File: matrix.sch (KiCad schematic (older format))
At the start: 134 parts, among them SW1 SW_Push, SW10 SW_Push, SW11 SW_Push, SW12 SW_Push, SW13 SW_Push, SW14 SW_Push, SW15 SW_Push, SW16 SW_Push, SW17 SW_Push, SW18 SW_Push, SW19 SW_Push, SW2 SW_Push, SW20 SW_Push, SW21 SW_Push, SW22 SW_Push, SW23 SW_Push, SW24 SW_Push, SW25 SW_Push, SW26 SW_Push, SW27 SW_Push, SW28 SW_Push, SW29 SW_Push, SW3 SW_Push, SW30 SW_Push, SW31 SW_Push, SW32 SW_Push, SW33 SW_Push, SW34 SW_Push, SW35 SW_Push, SW36 SW_Push, SW37 SW_Push, SW38 SW_Push, SW39 SW_Push, SW4 SW_Push, SW40 SW_Push, SW41 SW_Push, SW42 SW_Push, SW43 SW_Push, SW44 SW_Push, SW45 SW_Push, SW46 SW_Push, SW47 SW_Push, SW48 SW_Push, SW49 SW_Push, SW5 SW_Push, SW50 SW_Push, SW51 SW_Push, SW52 SW_Push, SW53 SW_Push, SW54 SW_Push, SW55 SW_Push, SW56 SW_Push, SW57 SW_Push, SW58 SW_Push, SW59 SW_Push, SW6 SW_Push, SW60 SW_Push, SW61 SW_Push, SW62 SW_Push, SW63 SW_Push, SW64 SW_Push, SW65 SW_Push, SW66 SW_Push, SW67 SW_Push, SW7 SW_Push, SW8 SW_Push, SW9 SW_Push

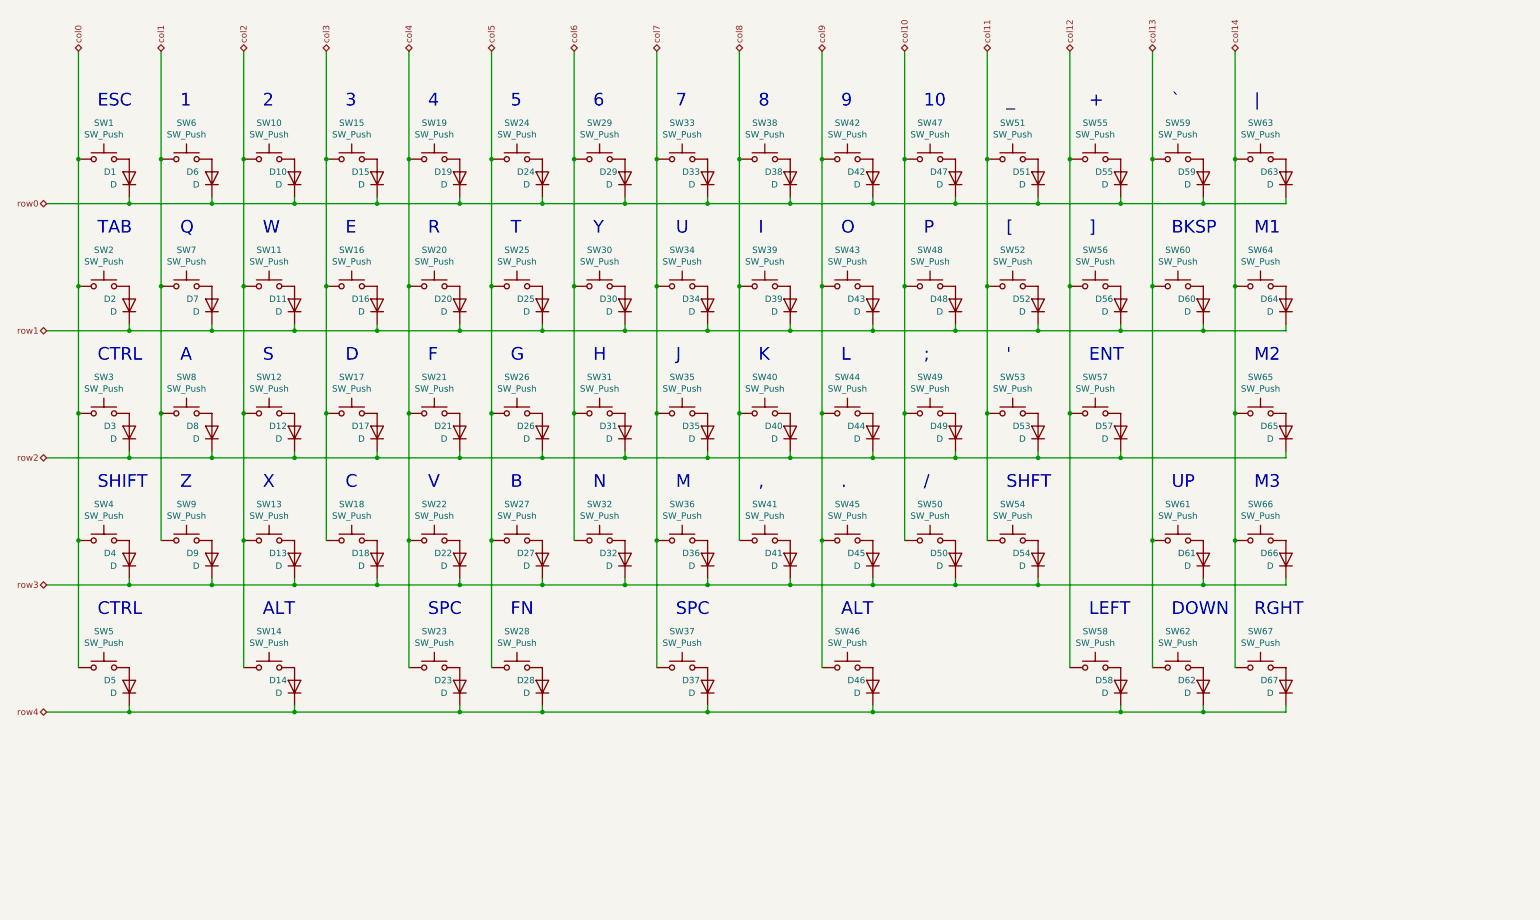
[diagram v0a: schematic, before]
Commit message: Initial project update
- Imported FateParts library
- Updated schematic with full backspace switch and stepped capslock switch
- Added new switch footprints to layout
- Updated some traces in layout
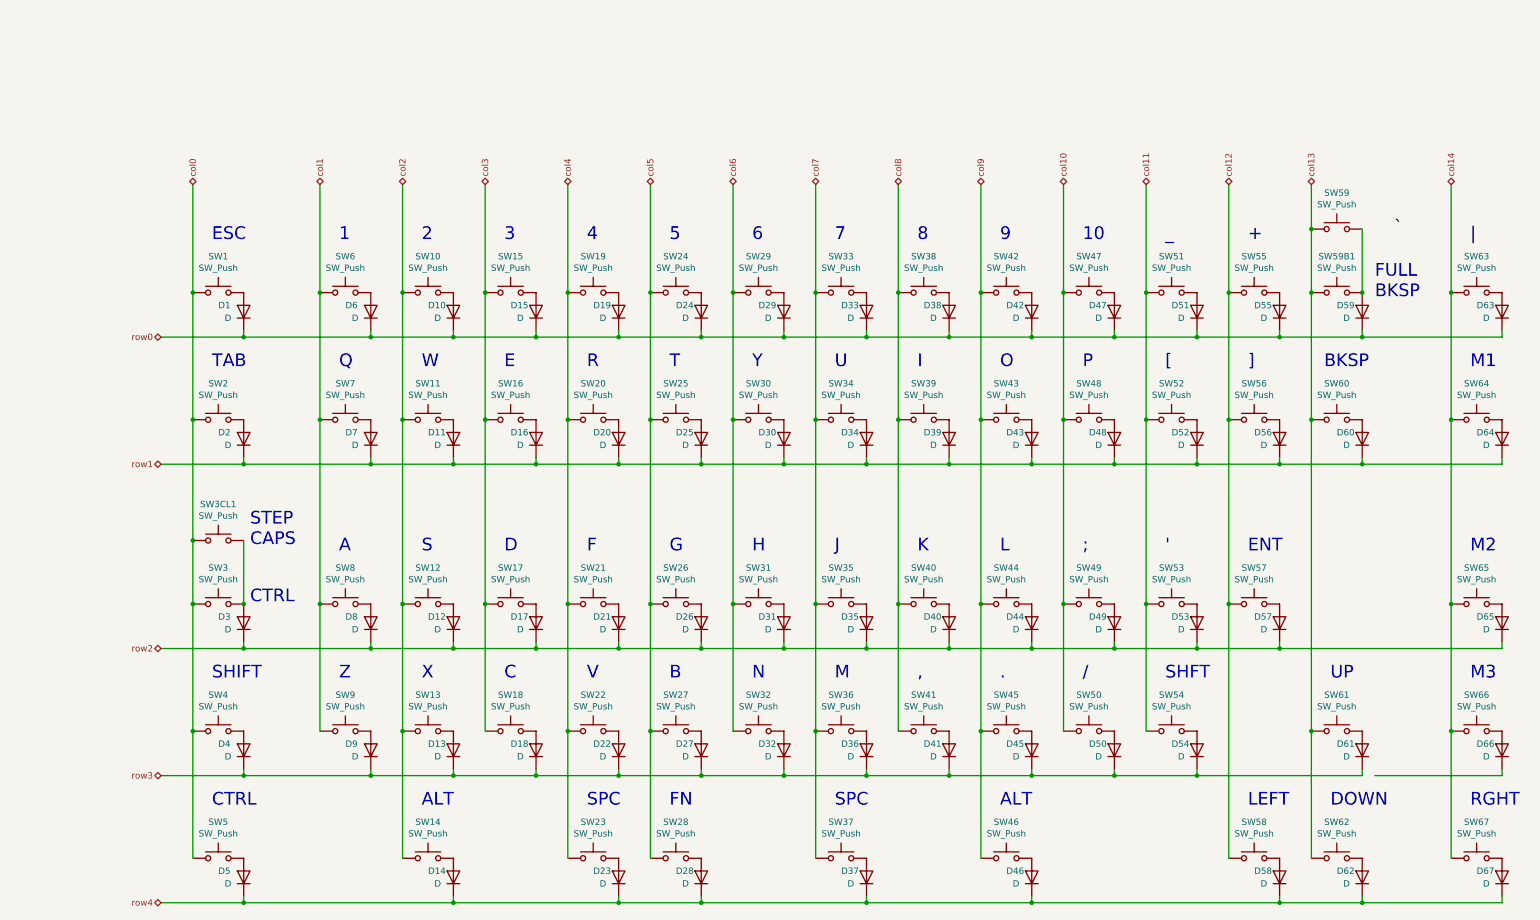
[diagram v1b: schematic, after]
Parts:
- added SW3CL1: SW_Push, FateParts-MXSwitch:SW_Cherry_MX_1.25u_PCB, symbol Switch:SW_Push
- added SW59B1: SW_Push, FateParts-MXSwitch:SW_Cherry_MX_2.00u_PCB, symbol Switch:SW_Push
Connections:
- net col0: now also SW3CL1.1
- net col13: now also SW59B1.1
- net row3: no longer D66.1 (K)
- net at D3.2 (A), SW3.2: now also SW3CL1.2
- net at D59.2 (A), SW59.2: now also SW59B1.2
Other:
- note added: "FULL\nBKSP"
- note added: "STEP\nCAPS"
- moved on the sheet: D1, D10, D11, D12, D13, D14, D15, D16, D17, D18, D19, D2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

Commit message: Addition of BOM and position files
- Added JLCPCB part numbers in BOM and exported
- Exported component positioning file
- Some minor cleanup of traces and silkscreen legend positions.
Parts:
- D1, D10, D11, D12, D13, D14, D15, D16, D17, D18, D19, D2, D20, D21, D22, D23, D24, D25, D26, D27, D28, D29, D3, D30, D31, D32, D33, D34, D35, D36, D37, D38, D39, D4, D40, D41, D42, D43, D44, D45, D46, D47, D48, D49, D5, D50, D51, D52, D53, D54, D55, D56, D57, D58, D59, D6, D60, D61, D62, D63, D64, D65, D66, D67, D7, D8, D9: LCSC (none) -> C81598
